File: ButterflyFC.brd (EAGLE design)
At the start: 36.1 x 36.5 mm, 7 parts

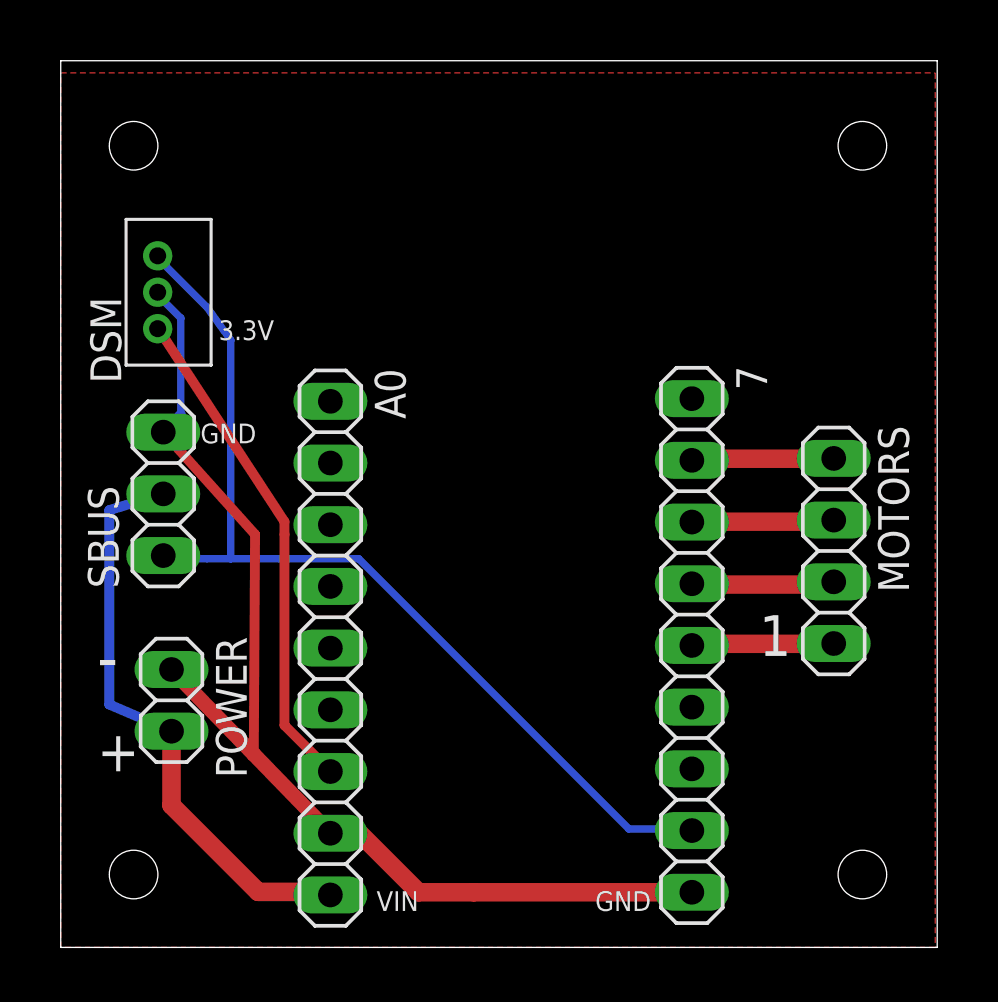
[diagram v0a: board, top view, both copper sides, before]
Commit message: Aligned / expaneded mounting holes
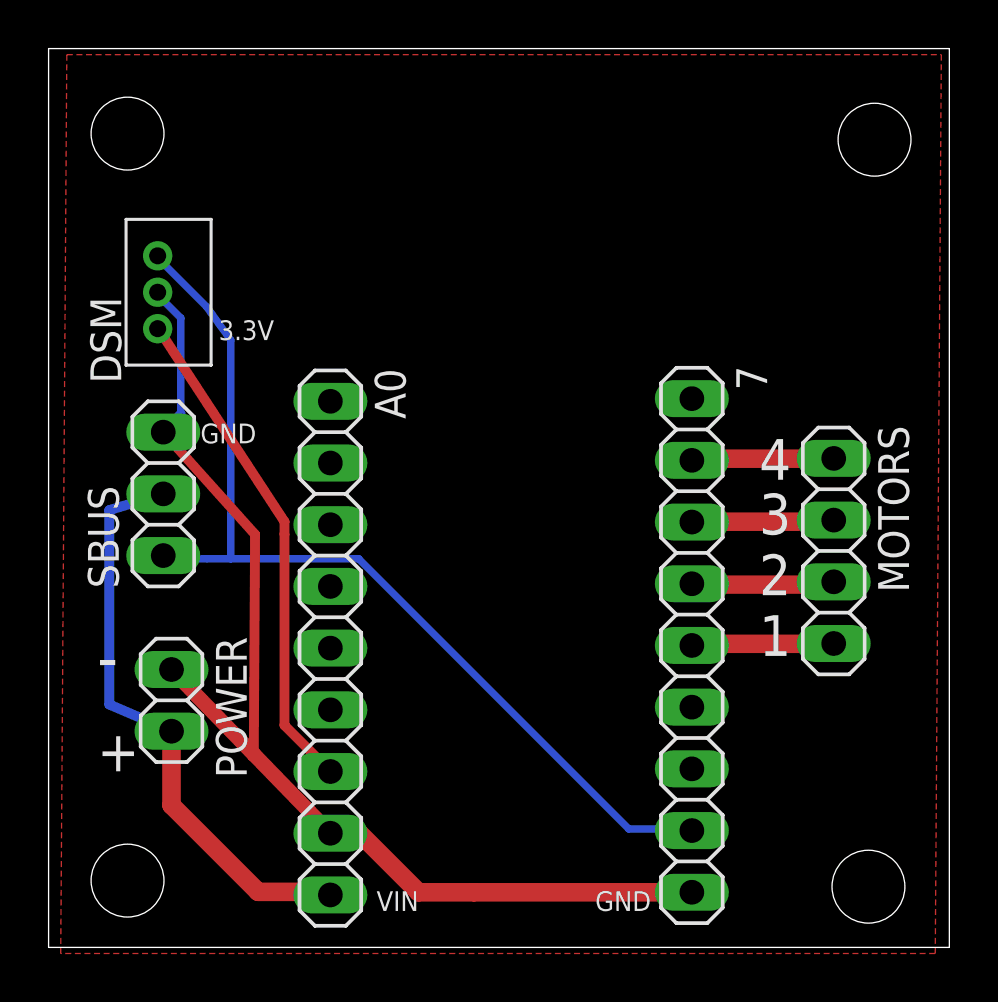
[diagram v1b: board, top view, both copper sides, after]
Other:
- board size 36.1 x 36.5 mm -> 37.1 x 37 mm
- board text added: "2"
- board text added: "3"
- board text added: "4"
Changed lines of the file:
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@@
 <board>
 <plain>
-<wire x1="1" y1="0" x2="37.08" y2="0" width="0" layer="20"/>
-<wire x1="37.08" y1="0" x2="37.08" y2="36.5" width="0" layer="20"/>
-<wire x1="37.08" y1="36.5" x2="1" y2="36.5" width="0" layer="20"/>
-<wire x1="1" y1="36.5" x2="1" y2="0" width="0" layer="20"/>
-<hole x="4" y="3" drill="2"/>
-<hole x="4" y="33" drill="2"/>
-<hole x="34" y="33" drill="2"/>
-<hole x="34" y="3" drill="2"/>
+<wire x1="0.5" y1="0" x2="37.58" y2="0" width="0" layer="20"/>
+<wire x1="37.58" y1="0" x2="37.58" y2="37" width="0" layer="20"/>
+<wire x1="37.58" y1="37" x2="0.5" y2="37" width="0" layer="20"/>
+<wire x1="0.5" y1="37" x2="0.5" y2="0" width="0" layer="20"/>
+<hole x="3.75" y="2.75" drill="3"/>
+<hole x="3.75" y="33.5" drill="3"/>
+<hole x="34.5" y="33.25" drill="3"/>
+<hole x="34.25" y="2.5" drill="3"/>
 <text x="14" y="1.5" size="0.8128" layer="21">VIN</text>
 <text x="23" y="1.5" size="0.8128" layer="21">GND</text>
@@
 <text x="2.5" y="11" size="1.9304" layer="21">-</text>
 <text x="6.75" y="20.75" size="0.8128" layer="21">GND</text>
+<text x="29.75" y="14.5" size="1.6764" layer="21">2</text>
+<text x="29.75" y="17" size="1.6764" layer="21">3</text>
+<text x="29.75" y="19.25" size="1.6764" layer="21">4</text>
 </plain>
 <attributes>
@@
 <wire x1="9" y1="17" x2="8.947425" y2="7.948984375" width="0.4064" layer="1"/>
 <polygon width="0.4064" layer="1">
-<vertex x="1" y="36"/>
-<vertex x="37" y="36"/>
-<vertex x="37" y="0"/>
-<vertex x="1" y="0"/>
+<vertex x="1.25" y="36.75"/>
+<vertex x="37.25" y="36.75"/>
+<vertex x="37" y="-0.25"/>
+<vertex x="1" y="-0.25"/>
 </polygon>
 </signal>

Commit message: Adjusted Butterfly board mounting hole positions
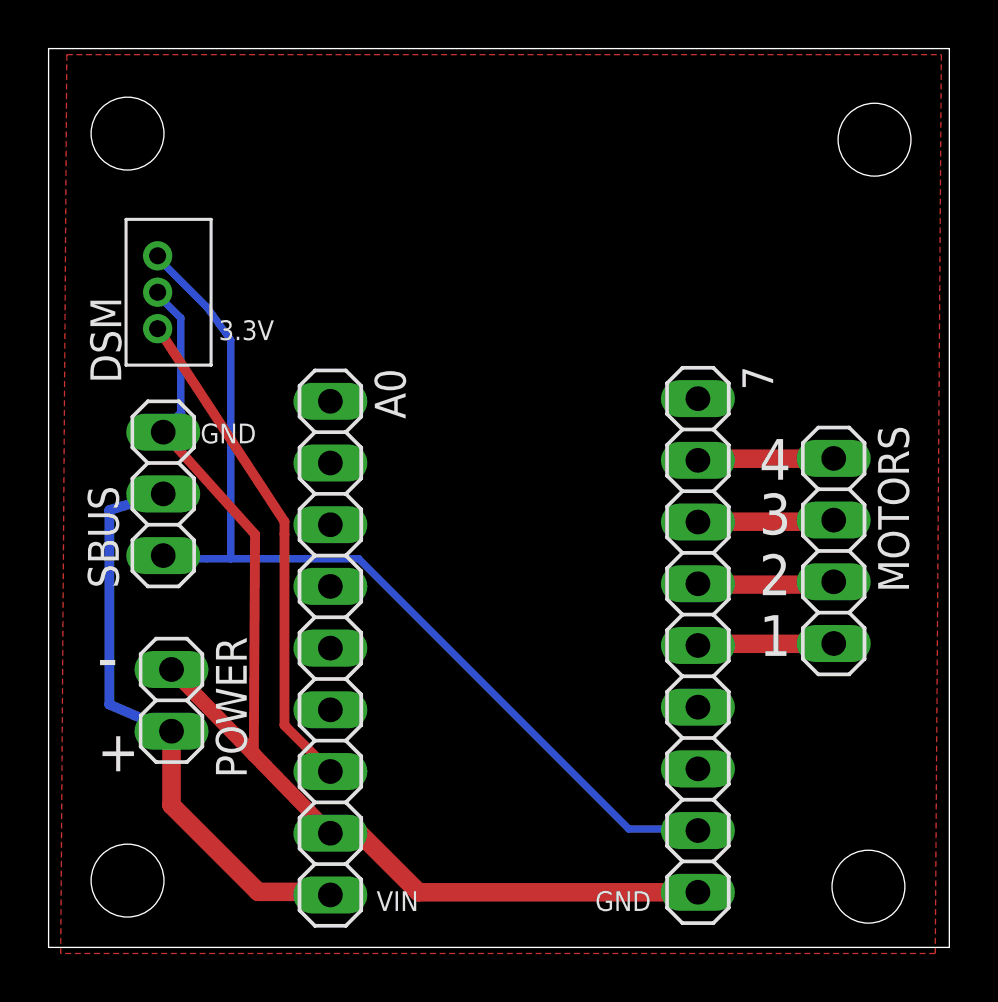
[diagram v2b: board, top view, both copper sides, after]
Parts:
- moved 7 0.25 mm to (27.2, 12.4)
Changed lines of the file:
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@@
 </autorouter>
 <elements>
-<element name="7" library="pinhead" library_urn="urn:adsk.eagle:library:325" package="1X09" package3d_urn="urn:adsk.eagle:package:22483/2" value="" x="26.98" y="12.43" rot="R270"/>
+<element name="7" library="pinhead" library_urn="urn:adsk.eagle:library:325" package="1X09" package3d_urn="urn:adsk.eagle:package:22483/2" value="" x="27.23" y="12.43" rot="R270"/>
 <element name="A0" library="pinhead" library_urn="urn:adsk.eagle:library:325" package="1X09" package3d_urn="urn:adsk.eagle:package:22483/2" value="" x="12.1" y="12.32" rot="R270"/>
 <element name="DSM" library="jst" package="B3B-ZR" value="B3B-ZR" x="4.99" y="26.97" rot="R90"/>
@@
 <contactref element="SBUS" pad="3"/>
 <contactref element="7" pad="9"/>
-<wire x1="26.9748" y1="2.286" x2="26.98" y2="2.27" width="0.1524" layer="1"/>
-<wire x1="26.98" y1="2.27" x2="18" y2="2.27" width="0.762" layer="1"/>
-<wire x1="18" y1="2.27" x2="15.73" y2="2.27" width="0.762" layer="1"/>
+<wire x1="26.9748" y1="2.286" x2="27.23" y2="2.27" width="0.1524" layer="1"/>
+<wire x1="27.23" y1="2.27" x2="15.73" y2="2.27" width="0.762" layer="1"/>
 <wire x1="13" y1="5" x2="15.73" y2="2.27" width="0.762" layer="1"/>
 <wire x1="12.4" y1="5" x2="13" y2="5" width="0.762240625" layer="1"/>
@@
 <contactref element="MOTORS" pad="1"/>
 <wire x1="33.6804" y1="20.1168" x2="27.1272" y2="20.1168" width="0.762" layer="1"/>
-<wire x1="27.1272" y1="20.1168" x2="26.98" y2="20.05" width="0.1524" layer="1"/>
+<wire x1="27.1272" y1="20.1168" x2="27.23" y2="20.05" width="0.1524" layer="1"/>
 <wire x1="33.6804" y1="20.1168" x2="32.82" y2="20.13" width="0.1524" layer="1"/>
 </signal>
@@
 <contactref element="MOTORS" pad="2"/>
 <wire x1="33.6804" y1="17.526" x2="27.1272" y2="17.526" width="0.762" layer="1"/>
-<wire x1="27.1272" y1="17.526" x2="26.98" y2="17.51" width="0.1524" layer="1"/>
+<wire x1="27.1272" y1="17.526" x2="27.23" y2="17.51" width="0.1524" layer="1"/>
 <wire x1="33.6804" y1="17.526" x2="32.82" y2="17.59" width="0.1524" layer="1"/>
 </signal>
@@
 <contactref element="MOTORS" pad="3"/>
 <wire x1="33.6804" y1="14.9352" x2="27.1272" y2="14.9352" width="0.762" layer="1"/>
-<wire x1="27.1272" y1="14.9352" x2="26.98" y2="14.97" width="0.1524" layer="1"/>
+<wire x1="27.1272" y1="14.9352" x2="27.23" y2="14.97" width="0.1524" layer="1"/>
 <wire x1="33.6804" y1="14.9352" x2="32.82" y2="15.05" width="0.1524" layer="1"/>
 </signal>
@@
 <contactref element="MOTORS" pad="4"/>
 <wire x1="33.6804" y1="12.4968" x2="27.1272" y2="12.4968" width="0.762" layer="1"/>
-<wire x1="27.1272" y1="12.4968" x2="26.98" y2="12.43" width="0.1524" layer="1"/>
+<wire x1="27.1272" y1="12.4968" x2="27.23" y2="12.43" width="0.1524" layer="1"/>
 <wire x1="33.6804" y1="12.4968" x2="32.82" y2="12.51" width="0.1524" layer="1"/>
 </signal>
@@
 <wire x1="24.384" y1="4.8768" x2="26.9748" y2="4.8768" width="0.3048" layer="16"/>
 <wire x1="24.384" y1="4.8768" x2="13.2588" y2="16.002" width="0.3048" layer="16"/>
-<wire x1="26.9748" y1="4.8768" x2="26.98" y2="4.81" width="0.1524" layer="16"/>
+<wire x1="26.9748" y1="4.8768" x2="27.23" y2="4.81" width="0.1524" layer="16"/>
 <wire x1="13.2588" y1="16.002" x2="10" y2="16.001103125" width="0.3048" layer="16"/>
 <wire x1="10" y1="16.001103125" x2="8" y2="16.00055" width="0.3048" layer="16"/>
